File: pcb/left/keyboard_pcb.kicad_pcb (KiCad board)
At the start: 2 copper layers, 138.8 x 89.9 mm, 36 parts, among them J2 USB_C_Receptacle_USB2.0_16P, K00 KEYSW, K01 KEYSW, K02 KEYSW, K03 KEYSW, K04 KEYSW, K05 KEYSW, K10 KEYSW, K11 KEYSW, K12 KEYSW, K13 KEYSW, K14 KEYSW, K15 KEYSW, K20 KEYSW, K21 KEYSW, K22 KEYSW, K23 KEYSW, K24 KEYSW, K25 KEYSW, K30 KEYSW, K31 KEYSW, K32 KEYSW, U2 Pico

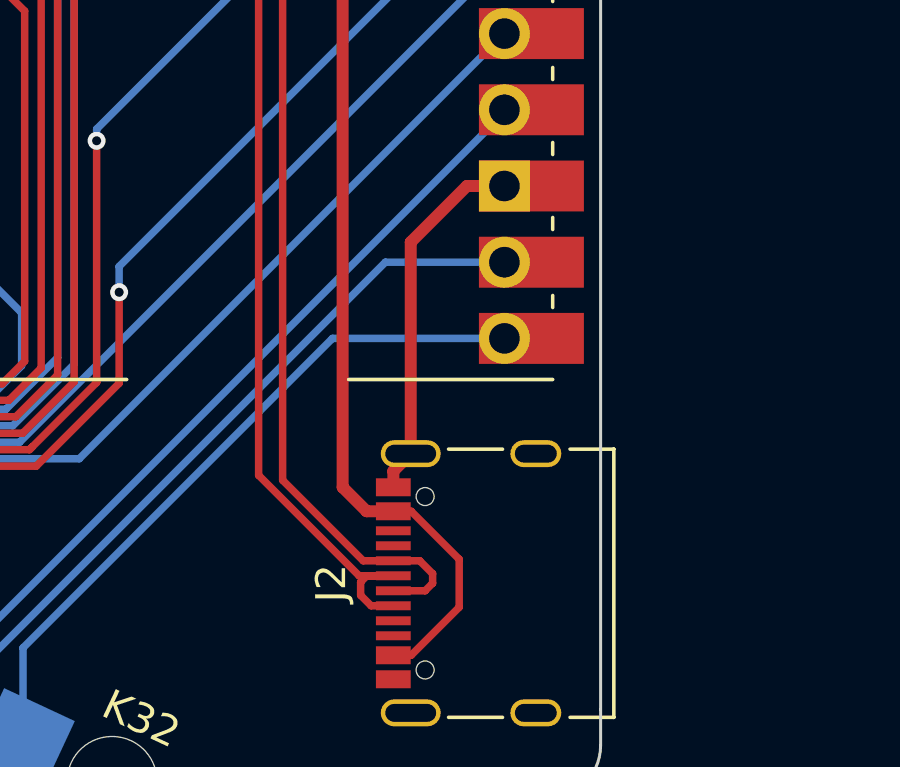
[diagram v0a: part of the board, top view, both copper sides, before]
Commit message: Add right side, add fabrication outputs
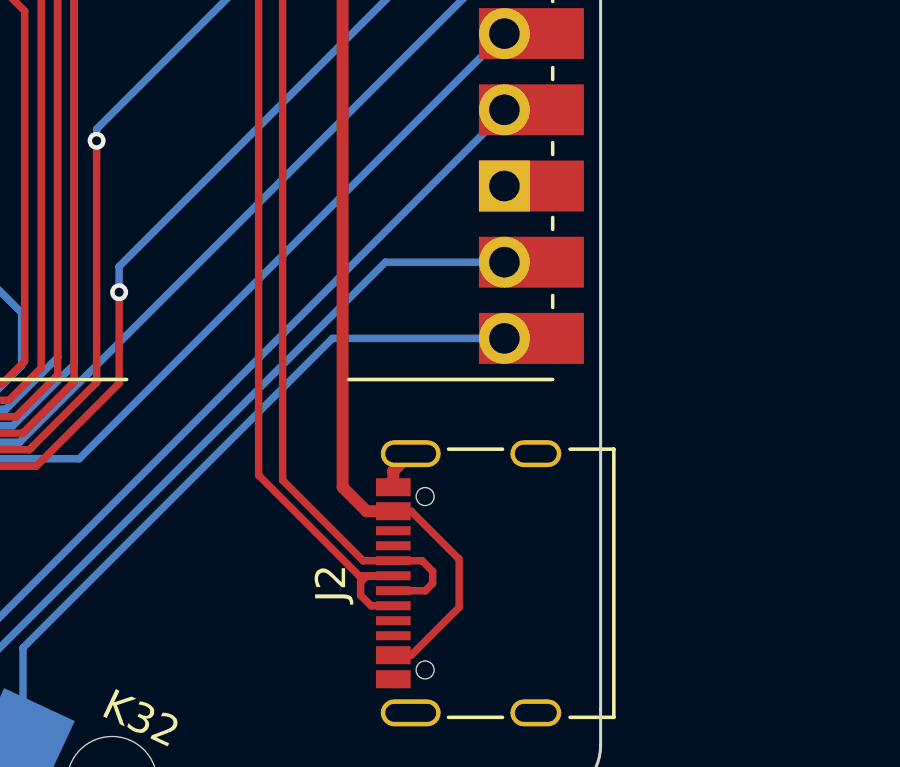
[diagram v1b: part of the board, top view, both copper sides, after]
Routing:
- net GND: track 42.1 -> 31.1 mm
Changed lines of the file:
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@@
 			(drillshape 0)
 			(scaleselection 1)
-			(outputdirectory "./gerber")
+			(outputdirectory "../fabrication/left/")
 		)
 	)
@@
 		)
 		(fp_line
-			(start -2.000001 -4.2)
+			(start -2.000002 -4.2)
 			(end -1.5 -3.7)
 			(stroke
@@
 		)
 		(fp_line
-			(start -2.000001 -4.2)
+			(start -2.000002 -4.2)
 			(end -1.5 -3.7)
 			(stroke
@@
 		(fp_arc
 			(start 0.999999 -3.7)
-			(mid 2.06066 -3.26066)
+			(mid 2.060659 -3.260661)
 			(end 2.500001 -2.2)
 			(stroke
@@
 		(fp_arc
 			(start 0.999999 -3.7)
-			(mid 2.06066 -3.26066)
+			(mid 2.060659 -3.260661)
 			(end 2.500001 -2.2)
 			(stroke
@@
 		(fp_line
 			(start 2.5 -1.5)
-			(end 7.000001 -1.5)
+			(end 7.000002 -1.5)
 			(stroke
 				(width 0.15)
@@
 		)
 		(fp_line
-			(start 7.000001 -1.5)
+			(start 7.000002 -1.5)
 			(end 7 -2)
 			(stroke
@@
 		(fp_line
 			(start 2.5 -1.5)
-			(end 7.000001 -1.5)
+			(end 7.000002 -1.5)
 			(stroke
 				(width 0.15)
@@
 		)
 		(fp_line
-			(start 7.000001 -1.5)
+			(start 7.000002 -1.5)
 			(end 7 -6.2)
 			(stroke
@@
 	)
 	(segment
-		(start 199.5932 95.758)
-		(end 198.3432 95.758)
-		(width 0.4)
-		(layer "F.Cu")
-		(net 1)
-	)
-	(segment
 		(start 195.89 105.26)
 		(end 195.89 105.7)
@@
 		(net 1)
 	)
-	(segment
-		(start 198.3432 95.758)
-		(end 196.47 97.6312)
-		(width 0.4)
-		(layer "F.Cu")
-		(net 1)
-	)
-	(segment
-		(start 196.47 97.6312)
-		(end 196.47 104.68)
-		(width 0.4)
-		(layer "F.Cu")
-		(net 1)
-	)
 	(via
 		(at 89.5 94)
@@
 	)
 	(segment
-		(start 195.15 109.75)
-		(end 195.89 109.75)
+		(start 194.8 108.96)
+		(end 194.8 109.4)
 		(width 0.25)
 		(layer "F.Cu")
@@
 	)
 	(segment
-		(start 194.8 108.96)
-		(end 194.8 109.4)
+		(start 195.15 109.75)
+		(end 195.89 109.75)
 		(width 0.25)
 		(layer "F.Cu")
@@
 	)
 	(segment
-		(start 194.8 109.4)
-		(end 195.15 109.75)
+		(start 195.01 108.75)
+		(end 194.8 108.96)
 		(width 0.25)
 		(layer "F.Cu")
@@
 	)
 	(segment
-		(start 195.01 108.75)
-		(end 194.8 108.96)
+		(start 194.748604 108.75)
+		(end 195.89 108.75)
 		(width 0.25)
 		(layer "F.Cu")
@@
 	)
 	(segment
-		(start 194.748604 108.75)
-		(end 195.89 108.75)
+		(start 194.8 109.4)
+		(end 195.15 109.75)
 		(width 0.25)
 		(layer "F.Cu")
@@
 	)
 	(segment
-		(start 197.2 108.68)
-		(end 197.2 109)
+		(start 181.8132 52.578)
+		(end 192.2 62.9648)
 		(width 0.25)
 		(layer "F.Cu")
@@
 	)
 	(segment
-		(start 196.77 108.25)
-		(end 197.2 108.68)
+		(start 192.2 62.9648)
+		(end 192.2 105.565)
 		(width 0.25)
 		(layer "F.Cu")
@@
 	)
 	(segment
-		(start 181.8132 52.578)
-		(end 192.2 62.9648)
+		(start 196.85 108.25)
+		(end 197.2 108.6)
 		(width 0.25)
 		(layer "F.Cu")
@@
 	)
 	(segment
-		(start 195.89 108.25)
-		(end 196.77 108.25)
+		(start 197.2 109)
+		(end 196.95 109.25)
 		(width 0.25)
 		(layer "F.Cu")
@@
 	)
 	(segment
-		(start 192.2 62.9648)
-		(end 192.2 105.565)
+		(start 197.2 108.6)
+		(end 197.2 109)
 		(width 0.25)
 		(layer "F.Cu")
@@
 	)
 	(segment
-		(start 197.2 109)
-		(end 196.95 109.25)
+		(start 192.2 105.565)
+		(end 194.885 108.25)
 		(width 0.25)
 		(layer "F.Cu")
@@
 	)
 	(segment
-		(start 192.2 105.565)
-		(end 194.885 108.25)
+		(start 196.95 109.25)
+		(end 195.89 109.25)
 		(width 0.25)
 		(layer "F.Cu")
@@
 	)
 	(segment
-		(start 196.95 109.25)
-		(end 195.89 109.25)
+		(start 195.89 108.25)
+		(end 196.85 108.25)
 		(width 0.25)
 		(layer "F.Cu")
